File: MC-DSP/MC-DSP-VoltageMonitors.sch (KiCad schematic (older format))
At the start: 9 parts, among them U181 BU4831F-TR, U182 BU4847F-TR, U183 74ACT08SCX, U184 74LVC1G07QDCKTQ1

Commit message: ADC refs, FTDI changes, and more
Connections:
- net labels added: SafeState
- net labels removed: DSP_XRSn, GlobalReset
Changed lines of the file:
@@
 $Descr A4 11693 8268
 encoding utf-8
-Sheet 8 9
+Sheet 6 9
 Title ""
 Date ""
@@
 $EndComp
 Text HLabel 8250 3250 2    50   Input ~ 0
-GlobalReset
+SafeState
 Text Notes 4750 1550 0    50   ~ 0
 check if we really need 5V
@@
 Text Notes 6450 2350 0    50   ~ 0
 check RD to see if needs to go anywhere else
-Text HLabel 3000 3250 0    50   Input ~ 0
-DSP_XRSn
-Wire Wire Line
-	3000 3250 3600 3250
-Connection ~ 3600 3250
 Wire Wire Line
 	5900 3250 6950 3250
@@
 Text Notes 5150 4350 0    50   ~ 0
 XRS Vmonitors need to control GR\nGR needs to be able to pulll down XRS\nSLED contolled by XRS and Vmonitors
+Wire Wire Line
+	7250 3350 7250 3650
 $EndSCHEMATC

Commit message: All parts labeled, just need to pick passives basically.
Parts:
- removed R184: 10K, Resistor_SMD:R_0603_1608Metric, symbol Device:R_Small_US
- removed U182: BU4847F-TR, SOT130P210X105-4N, symbol BU4847F-TR:BU4847F-TR
- removed U183: 74ACT08SCX, Package_SO:SOIC-14_3.9x8.7mm_P1.27mm, symbol Existing_IC_Models:74ACT08SCX
- removed U184: 74LVC1G07QDCKTQ1, Package_TO_SOT_SMD:SOT-353_SC-70-5, symbol Existing_IC_Models:74LVC1G07QDCKTQ1
- added U13: BU4811G-TR, ?, symbol BU4847F-TR:BU4847F-TR
- C14: renamed from C182; value 1 uF -> 1uF; footprint Capacitor_SMD:C_0603_1608Metric -> Capacitor_SMD:C_0201_0603Metric_Pad0.64x0.40mm_HandSolder
- C15: renamed from C181; value 1 uF or unpop -> 1uF; footprint Capacitor_SMD:C_0603_1608Metric -> Capacitor_SMD:C_0201_0603Metric_Pad0.64x0.40mm_HandSolder
- C16: renamed from C?; value C -> 10nF; footprint Capacitor_SMD:C_0603_1608Metric -> Capacitor_SMD:C_0201_0603Metric_Pad0.64x0.40mm_HandSolder
- R18: renamed from R?; value R -> 10K; footprint Resistor_SMD:R_0603_1608Metric -> Resistor_SMD:R_0603_1608Metric_Pad0.98x0.95mm_HandSolder
- U12: renamed from U181; footprint SOT130P210X105-4N -> ?
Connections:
- net labels added: +1V2
- net labels removed: +5V
- wire segments 43 -> 21
- no-connect marks 0 -> 2
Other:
- note added: "check maximum open drain current, based on all pullups on all cards"
- note removed: "Add 1.2V voltage monitor"
- note removed: "Send to XRS on DSP"
- note removed: "check RD to see if needs to go anywhere else"
- note removed: "check if we really need 5V"
- moved on the sheet: C14, C15

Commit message: DSP - added footprints and links to most parts
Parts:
- U12: footprint ? -> mark_footprints:SOP4
- U13: footprint ? -> Package_SO:TSOP-5_1.65x3.05mm_P0.95mm
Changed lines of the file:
@@
 F 1 "1uF" H 5492 2405 50  0000 L CNN
 F 2 "Capacitor_SMD:C_0201_0603Metric_Pad0.64x0.40mm_HandSolder" H 5400 2450 50  0001 C CNN
-F 3 "?" H 5400 2450 50  0001 C CNN
+F 3 "https://www.digikey.com/en/products/detail/yageo/CC0603KRX7R9BB104/2103082" H 5400 2450 50  0001 C CNN
 	1    5400 2450
 	-1   0    0    -1
@@
 F 1 "1uF" H 3542 2405 50  0000 L CNN
 F 2 "Capacitor_SMD:C_0201_0603Metric_Pad0.64x0.40mm_HandSolder" H 3450 2450 50  0001 C CNN
-F 3 "?" H 3450 2450 50  0001 C CNN
+F 3 "https://www.digikey.com/en/products/detail/yageo/CC0603KRX7R9BB104/2103082" H 3450 2450 50  0001 C CNN
 	1    3450 2450
 	-1   0    0    -1
@@
 F 0 "U12" H 2600 2920 50  0000 C CNN
 F 1 "BU4831F-TR" H 2600 2829 50  0000 C CNN
-F 2 "?" H 2600 2350 50  0001 L BNN
+F 2 "mark_footprints:SOP4" H 2600 2350 50  0001 L BNN
 F 3 "https://www.mouser.com/ProductDetail/ROHM-Semiconductor/BU4831F-TR/?qs=IsRgwgmxh68BcBedREMXuQ%3D%3D" H 2600 2350 50  0001 L BNN
 F 4 "Rohm" H 2600 2350 50  0001 L BNN "Manufacturer"
@@
 	5550 3250 5550 2250
 $Comp
-L power:GND #PWR?
+L power:GND #PWR0165
 U 1 1 61B37580
 P 3400 2650
-F 0 "#PWR?" H 3400 2400 50  0001 C CNN
+F 0 "#PWR0165" H 3400 2400 50  0001 C CNN
 F 1 "GND" H 3405 2477 50  0000 C CNN
 F 2 "" H 3400 2650 50  0001 C CNN
@@
 $EndComp
 $Comp
-L power:GND #PWR?
+L power:GND #PWR0166
 U 1 1 61B38669
 P 5350 2650
-F 0 "#PWR?" H 5350 2400 50  0001 C CNN
+F 0 "#PWR0166" H 5350 2400 50  0001 C CNN
 F 1 "GND" H 5355 2477 50  0000 C CNN
 F 2 "" H 5350 2650 50  0001 C CNN
@@
 $EndComp
 $Comp
-L power:+3V3 #PWR?
+L power:+3V3 #PWR0167
 U 1 1 61B77D23
 P 3400 2050
-F 0 "#PWR?" H 3400 1900 50  0001 C CNN
+F 0 "#PWR0167" H 3400 1900 50  0001 C CNN
 F 1 "+3V3" H 3415 2223 50  0000 C CNN
 F 2 "" H 3400 2050 50  0001 C CNN
@@
 Connection ~ 5550 3250
 $Comp
-L power:GND #PWR?
+L power:GND #PWR0168
 U 1 1 61F53067
 P 5850 3450
-F 0 "#PWR?" H 5850 3200 50  0001 C CNN
+F 0 "#PWR0168" H 5850 3200 50  0001 C CNN
 F 1 "GND" H 5855 3277 50  0000 C CNN
 F 2 "" H 5850 3450 50  0001 C CNN
@@
 	5900 2950 5900 3050
 $Comp
-L power:+3V3 #PWR?
+L power:+3V3 #PWR0169
 U 1 1 61F51CC0
 P 5900 2950
-F 0 "#PWR?" H 5900 2800 50  0001 C CNN
+F 0 "#PWR0169" H 5900 2800 50  0001 C CNN
 F 1 "+3V3" H 5915 3123 50  0000 C CNN
 F 2 "" H 5900 2950 50  0001 C CNN
@@
 F 1 "10nF" H 5942 3305 50  0000 L CNN
 F 2 "Capacitor_SMD:C_0201_0603Metric_Pad0.64x0.40mm_HandSolder" H 5850 3350 50  0001 C CNN
-F 3 "?" H 5850 3350 50  0001 C CNN
+F 3 "https://www.digikey.com/en/products/detail/kemet/C0603X103J4HAC7867/8334457" H 5850 3350 50  0001 C CNN
 	1    5850 3350
 	1    0    0    -1
@@
 F 1 "10K" H 5968 3105 50  0000 L CNN
 F 2 "Resistor_SMD:R_0603_1608Metric_Pad0.98x0.95mm_HandSolder" H 5900 3150 50  0001 C CNN
-F 3 "?" H 5900 3150 50  0001 C CNN
+F 3 "https://www.digikey.com/en/products/detail/yageo/RC0603FR-0710KL/726880?s=N4IgTCBcDaIEoGEAMA2JBmAYnAtEg7AIxIDSAMiALoC%2BQA" H 5900 3150 50  0001 C CNN
 	1    5900 3150
 	1    0    0    -1
@@
 F 0 "U13" H 4550 2920 50  0000 C CNN
 F 1 "BU4811G-TR" H 4550 2829 50  0000 C CNN
-F 2 "?" H 4550 2350 50  0001 L BNN
+F 2 "Package_SO:TSOP-5_1.65x3.05mm_P0.95mm" H 4550 2350 50  0001 L BNN
 F 3 "https://www.mouser.com/ProductDetail/ROHM-Semiconductor/BU4811G-TR?qs=IsRgwgmxh68qDIZACyfaPg%3D%3D" H 4550 2350 50  0001 L BNN
 F 4 "" H 4550 2350 50  0001 L BNN "Manufacturer"
@@
 $EndComp
 $Comp
-L power:+1V2 #PWR?
+L power:+1V2 #PWR0170
 U 1 1 633B1389
 P 5350 2050
-F 0 "#PWR?" H 5350 1900 50  0001 C CNN
+F 0 "#PWR0170" H 5350 1900 50  0001 C CNN
 F 1 "+1V2" H 5365 2223 50  0000 C CNN
 F 2 "" H 5350 2050 50  0001 C CNN

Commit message: Removed clock buffer, misc leds, ethernet
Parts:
- C14, C15, C16: footprint Capacitor_SMD:C_0201_0603Metric_Pad0.64x0.40mm_HandSolder -> Capacitor_SMD:C_0603_1608Metric_Pad1.08x0.95mm_HandSolder
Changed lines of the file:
@@
 $Descr A4 11693 8268
 encoding utf-8
-Sheet 6 9
+Sheet 6 7
 Title ""
 Date ""
@@
 F 0 "C15" H 5492 2496 50  0000 L CNN
 F 1 "1uF" H 5492 2405 50  0000 L CNN
-F 2 "Capacitor_SMD:C_0201_0603Metric_Pad0.64x0.40mm_HandSolder" H 5400 2450 50  0001 C CNN
+F 2 "Capacitor_SMD:C_0603_1608Metric_Pad1.08x0.95mm_HandSolder" H 5400 2450 50  0001 C CNN
 F 3 "https://www.digikey.com/en/products/detail/yageo/CC0603KRX7R9BB104/2103082" H 5400 2450 50  0001 C CNN
 	1    5400 2450
@@
 F 0 "C14" H 3542 2496 50  0000 L CNN
 F 1 "1uF" H 3542 2405 50  0000 L CNN
-F 2 "Capacitor_SMD:C_0201_0603Metric_Pad0.64x0.40mm_HandSolder" H 3450 2450 50  0001 C CNN
+F 2 "Capacitor_SMD:C_0603_1608Metric_Pad1.08x0.95mm_HandSolder" H 3450 2450 50  0001 C CNN
 F 3 "https://www.digikey.com/en/products/detail/yageo/CC0603KRX7R9BB104/2103082" H 3450 2450 50  0001 C CNN
 	1    3450 2450
@@
 F 0 "C16" H 5942 3396 50  0000 L CNN
 F 1 "10nF" H 5942 3305 50  0000 L CNN
-F 2 "Capacitor_SMD:C_0201_0603Metric_Pad0.64x0.40mm_HandSolder" H 5850 3350 50  0001 C CNN
+F 2 "Capacitor_SMD:C_0603_1608Metric_Pad1.08x0.95mm_HandSolder" H 5850 3350 50  0001 C CNN
 F 3 "https://www.digikey.com/en/products/detail/kemet/C0603X103J4HAC7867/8334457" H 5850 3350 50  0001 C CNN
 	1    5850 3350

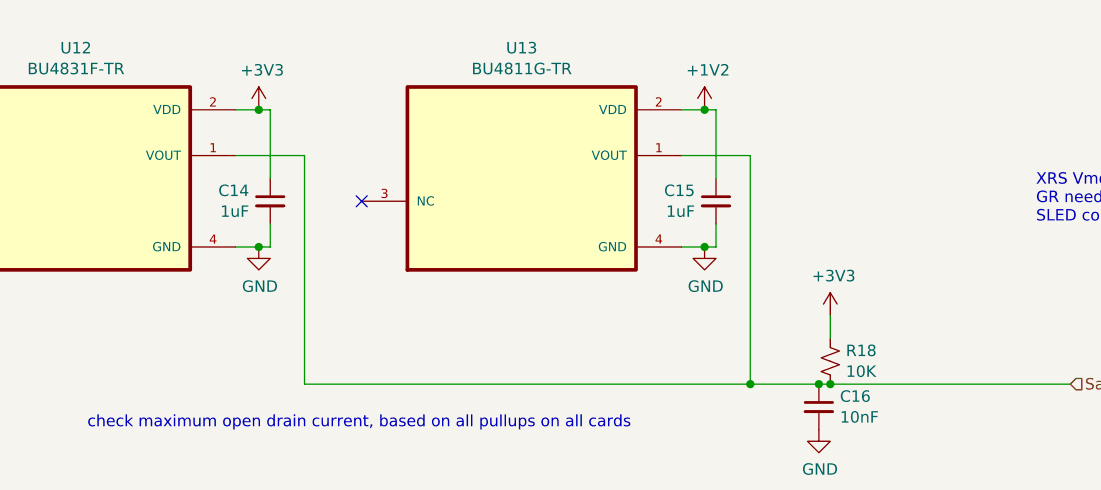
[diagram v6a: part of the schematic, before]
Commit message: Total overhaul of power planes. Routed whole Analog section, middle of digital section.
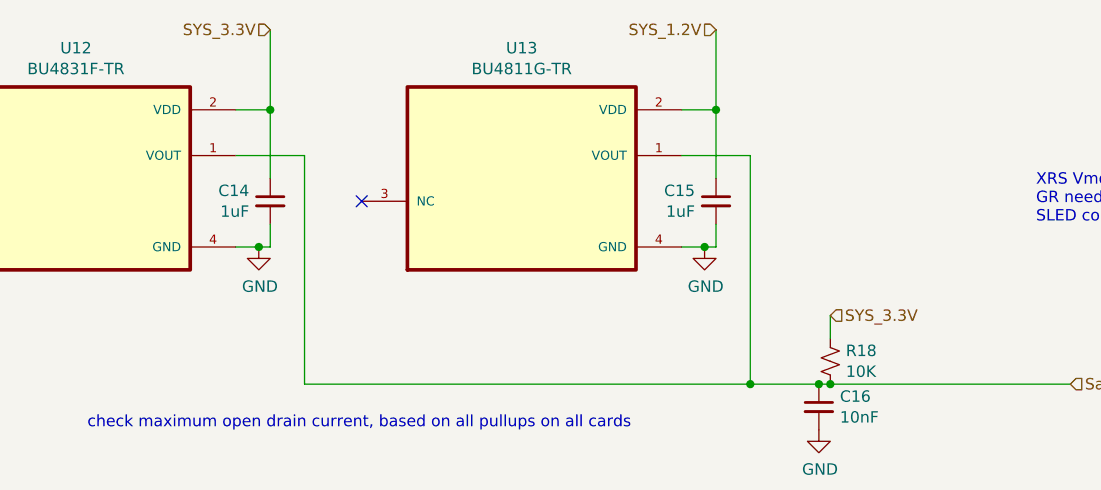
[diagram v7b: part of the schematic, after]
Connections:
- net +1V2 renamed SYS_1.2V
- net +3V3 renamed SYS_3.3V
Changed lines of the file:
@@
 $Descr A4 11693 8268
 encoding utf-8
-Sheet 3 7
+Sheet 6 7
 Title ""
 Date ""
@@
 	1    0    0    -1
 $EndComp
-$Comp
-L power:+3V3 #PWR0167
-U 1 1 61B77D23
-P 3400 2050
-F 0 "#PWR0167" H 3400 1900 50  0001 C CNN
-F 1 "+3V3" H 3415 2223 50  0000 C CNN
-F 2 "" H 3400 2050 50  0001 C CNN
-F 3 "" H 3400 2050 50  0001 C CNN
-	1    3400 2050
-	1    0    0    -1
-$EndComp
 Wire Wire Line
 	5250 2250 5550 2250
 Wire Wire Line
 	3300 2250 3600 2250
-Wire Wire Line
-	3300 2050 3400 2050
 Wire Wire Line
 	3600 2250 3600 3250
@@
 Wire Wire Line
 	5900 2950 5900 3050
-$Comp
-L power:+3V3 #PWR0169
-U 1 1 61F51CC0
-P 5900 2950
-F 0 "#PWR0169" H 5900 2800 50  0001 C CNN
-F 1 "+3V3" H 5915 3123 50  0000 C CNN
-F 2 "" H 5900 2950 50  0001 C CNN
-F 3 "" H 5900 2950 50  0001 C CNN
-	1    5900 2950
-	1    0    0    -1
-$EndComp
 Wire Wire Line
 	5850 3250 5550 3250
@@
 	1    0    0    -1
 $EndComp
-$Comp
-L power:+1V2 #PWR0170
-U 1 1 633B1389
-P 5350 2050
-F 0 "#PWR0170" H 5350 1900 50  0001 C CNN
-F 1 "+1V2" H 5365 2223 50  0000 C CNN
-F 2 "" H 5350 2050 50  0001 C CNN
-F 3 "" H 5350 2050 50  0001 C CNN
-	1    5350 2050
-	1    0    0    -1
-$EndComp
 Text Notes 2650 3450 0    50   ~ 0
 check maximum open drain current, based on all pullups on all cards
@@
 Wire Wire Line
 	3450 2350 3450 2050
-Wire Wire Line
-	3450 2050 3400 2050
 Wire Wire Line
 	5400 2650 5400 2550
@@
 Wire Wire Line
 	5250 2650 5350 2650
-Connection ~ 5350 2050
-Wire Wire Line
-	5350 2050 5400 2050
-Wire Wire Line
-	5250 2050 5350 2050
-Connection ~ 3400 2050
 NoConn ~ 3850 2450
 NoConn ~ 1900 2450
+Text HLabel 5400 1700 0    50   Input ~ 0
+SYS_1.2V
+Text HLabel 3450 1700 0    50   Input ~ 0
+SYS_3.3V
+Wire Wire Line
+	5250 2050 5400 2050
+Wire Wire Line
+	5400 2050 5400 1700
+Connection ~ 5400 2050
+Wire Wire Line
+	3300 2050 3450 2050
+Wire Wire Line
+	3450 2050 3450 1700
+Connection ~ 3450 2050
+Text HLabel 5900 2950 2    50   Input ~ 0
+SYS_3.3V
 $EndSCHEMATC
